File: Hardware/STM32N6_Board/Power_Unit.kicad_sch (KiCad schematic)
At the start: 72 parts, among them J1 Conn_01x02_Pin, J2 Conn_01x02_Pin, U1 STM32N657I0H3Q, U2 SPX5205-ADJ, U3 SPX5205-ADJ, U4 SPX5205-ADJ, U5 SPX5205-ADJ, U6 MC34064-ADJ-TR

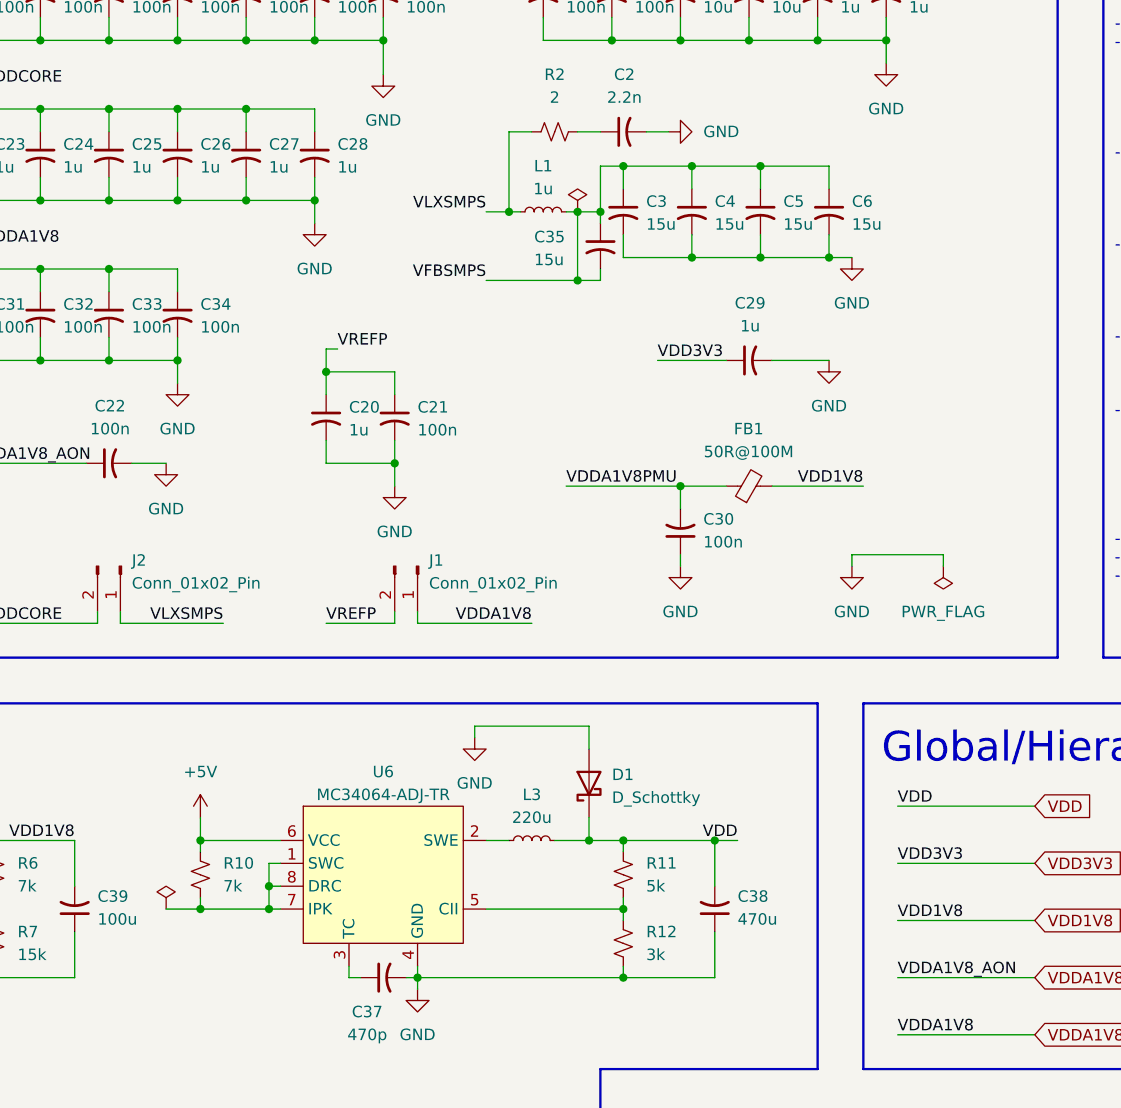
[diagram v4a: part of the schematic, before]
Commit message: Completed a lot of the layout of the STM Board
- Major layout complete, but all the wiring still left. 488 open nets!
- The STM32's BGA fanout is complete, now comes laying out traces
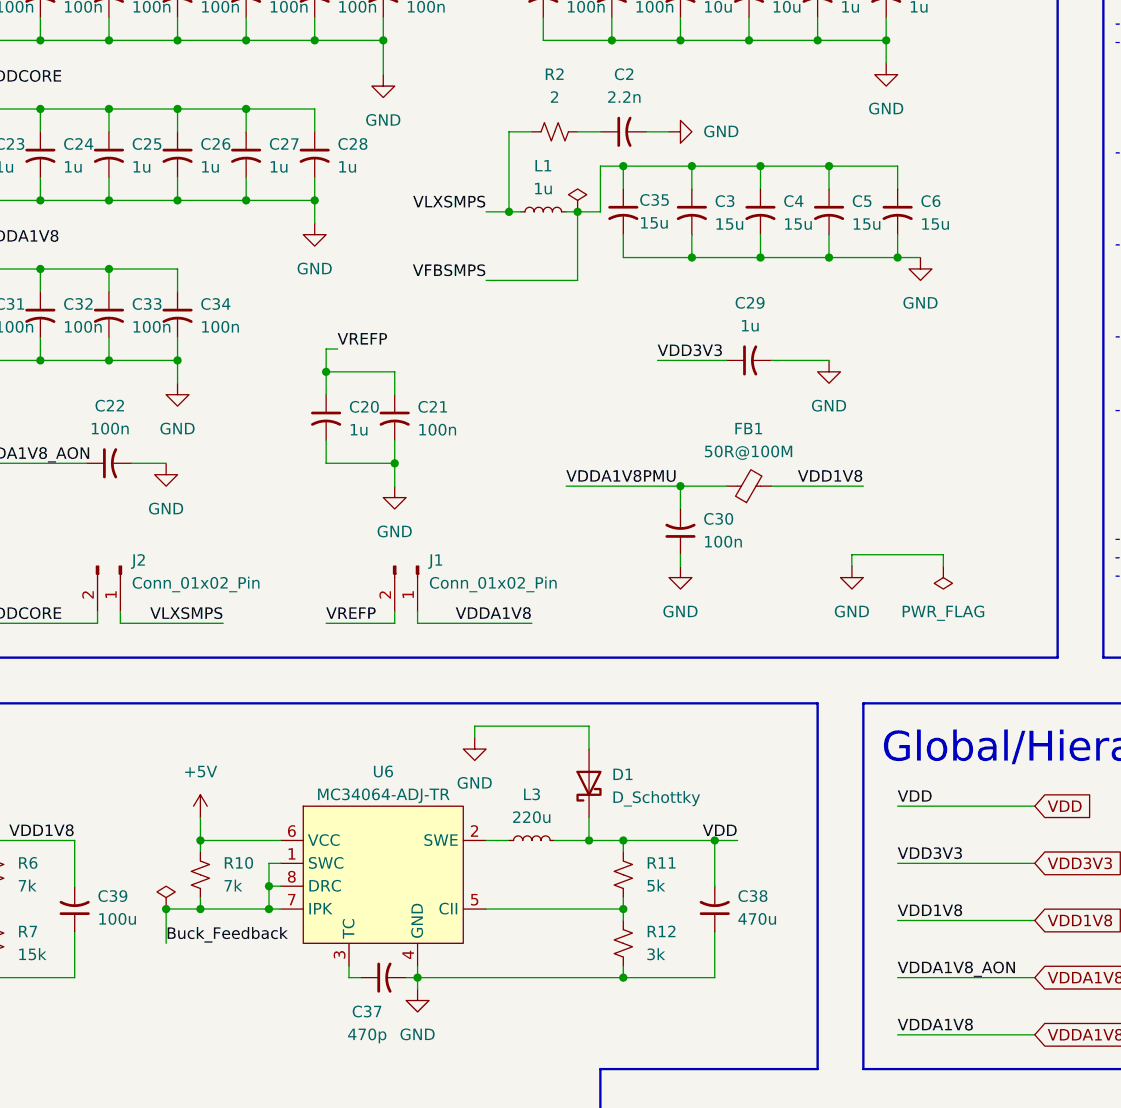
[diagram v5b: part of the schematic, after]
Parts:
- C1, C10, C11, C12, C13, C14, C15, C16, C17, C18, C19, C2, C20, C21, C22, C23, C24, C25, C26, C27, C28, C3, C30, C31, C32, C33, C34, C35, C37, C38, C4, C5, C6, C7, C8, C9: footprint Capacitor_SMD:C_0805_2012Metric_Pad1.18x1.45mm_HandSolder -> Capacitor_SMD:C_0402_1005Metric
- R18, R19: footprint Resistor_SMD:R_0805_2012Metric_Pad1.20x1.40mm_HandSolder -> Resistor_SMD:R_0402_1005Metric
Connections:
- net GND: now also C35.2
- net VFBSMPS: no longer C35.2
- net Buck_Feedback: now reaches R10.2, U6.1 (SWC), U6.7 (IPK), U6.8 (DRC)
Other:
- moved on the sheet: C3, C35, C4, C5, C6

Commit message: Added bypass capacitors to the STM32
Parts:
- R2: footprint Resistor_SMD:R_0805_2012Metric_Pad1.20x1.40mm_HandSolder -> Resistor_SMD:R_0402_1005Metric
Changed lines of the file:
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@@
 			)
 		)
-		(property "Footprint" "Resistor_SMD:R_0805_2012Metric_Pad1.20x1.40mm_HandSolder"
+		(property "Footprint" "Resistor_SMD:R_0402_1005Metric"
 			(at 167.64 57.15 0)
 			(effects
